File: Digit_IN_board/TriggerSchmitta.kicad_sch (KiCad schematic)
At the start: 6 parts, among them U5 HEF40106B, U6 HEF40106B, U7 HEF40106B

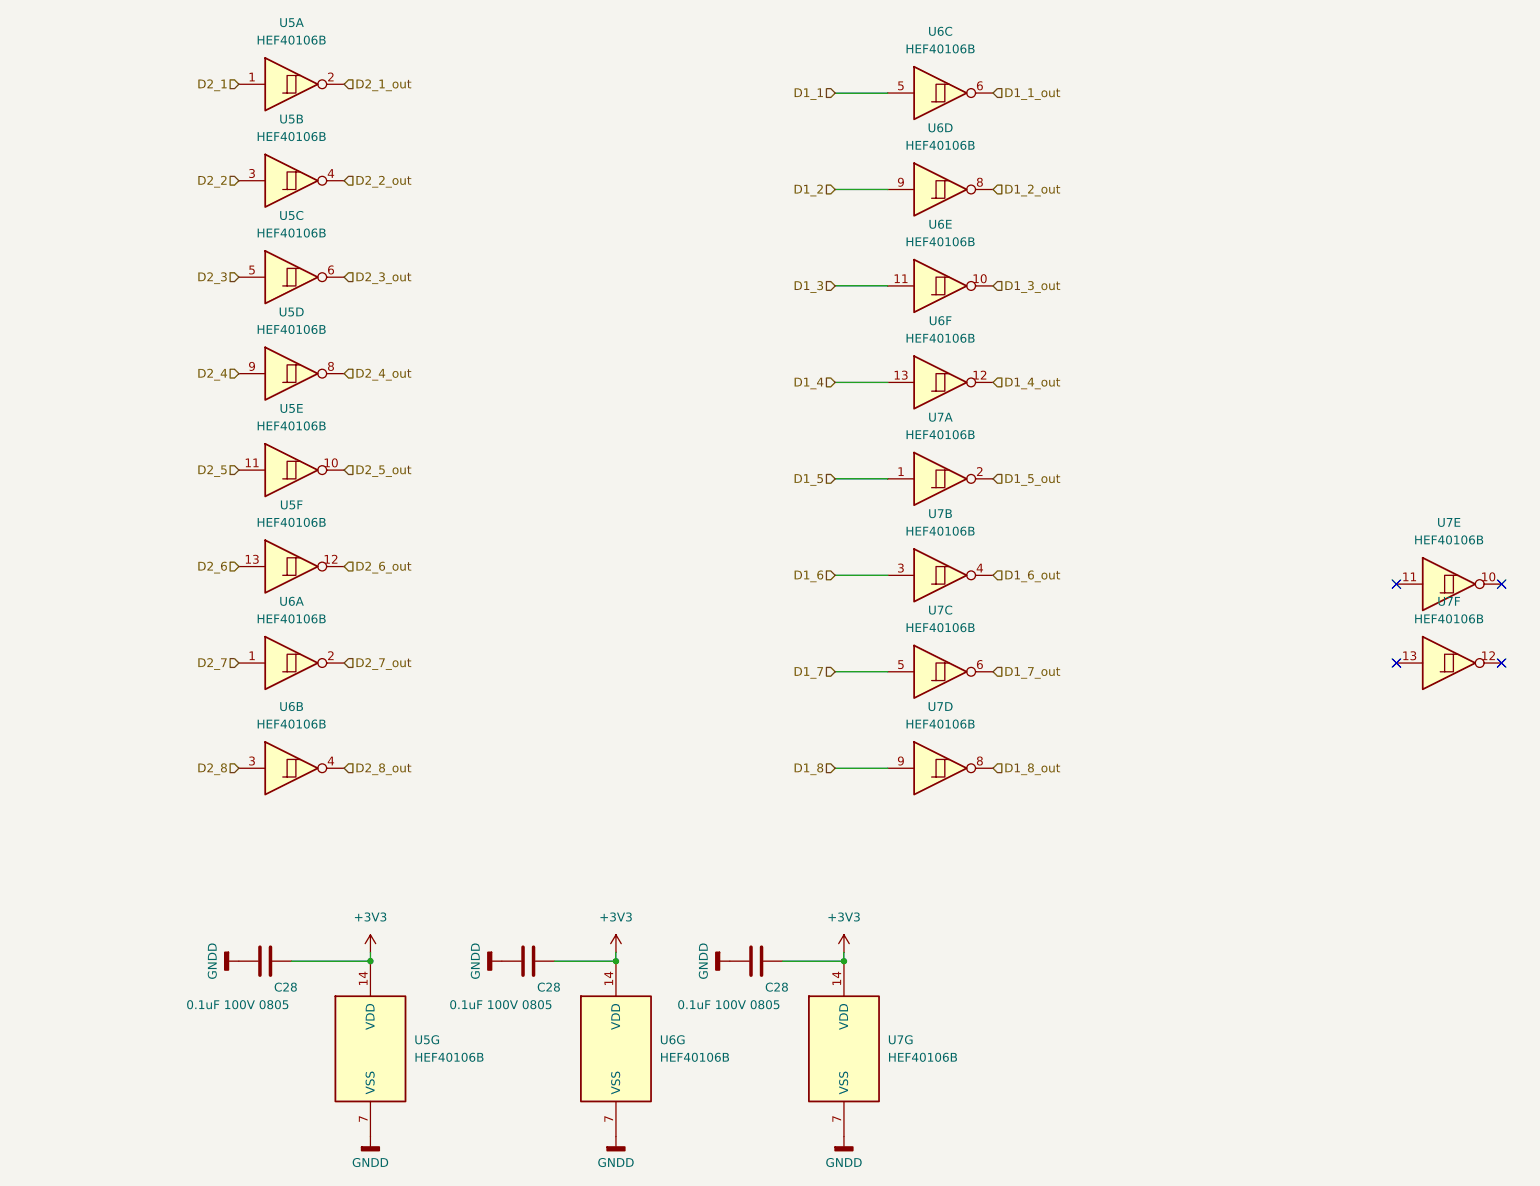
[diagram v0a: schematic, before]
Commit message: Modify Digit_IN, Motherbord, Step motors
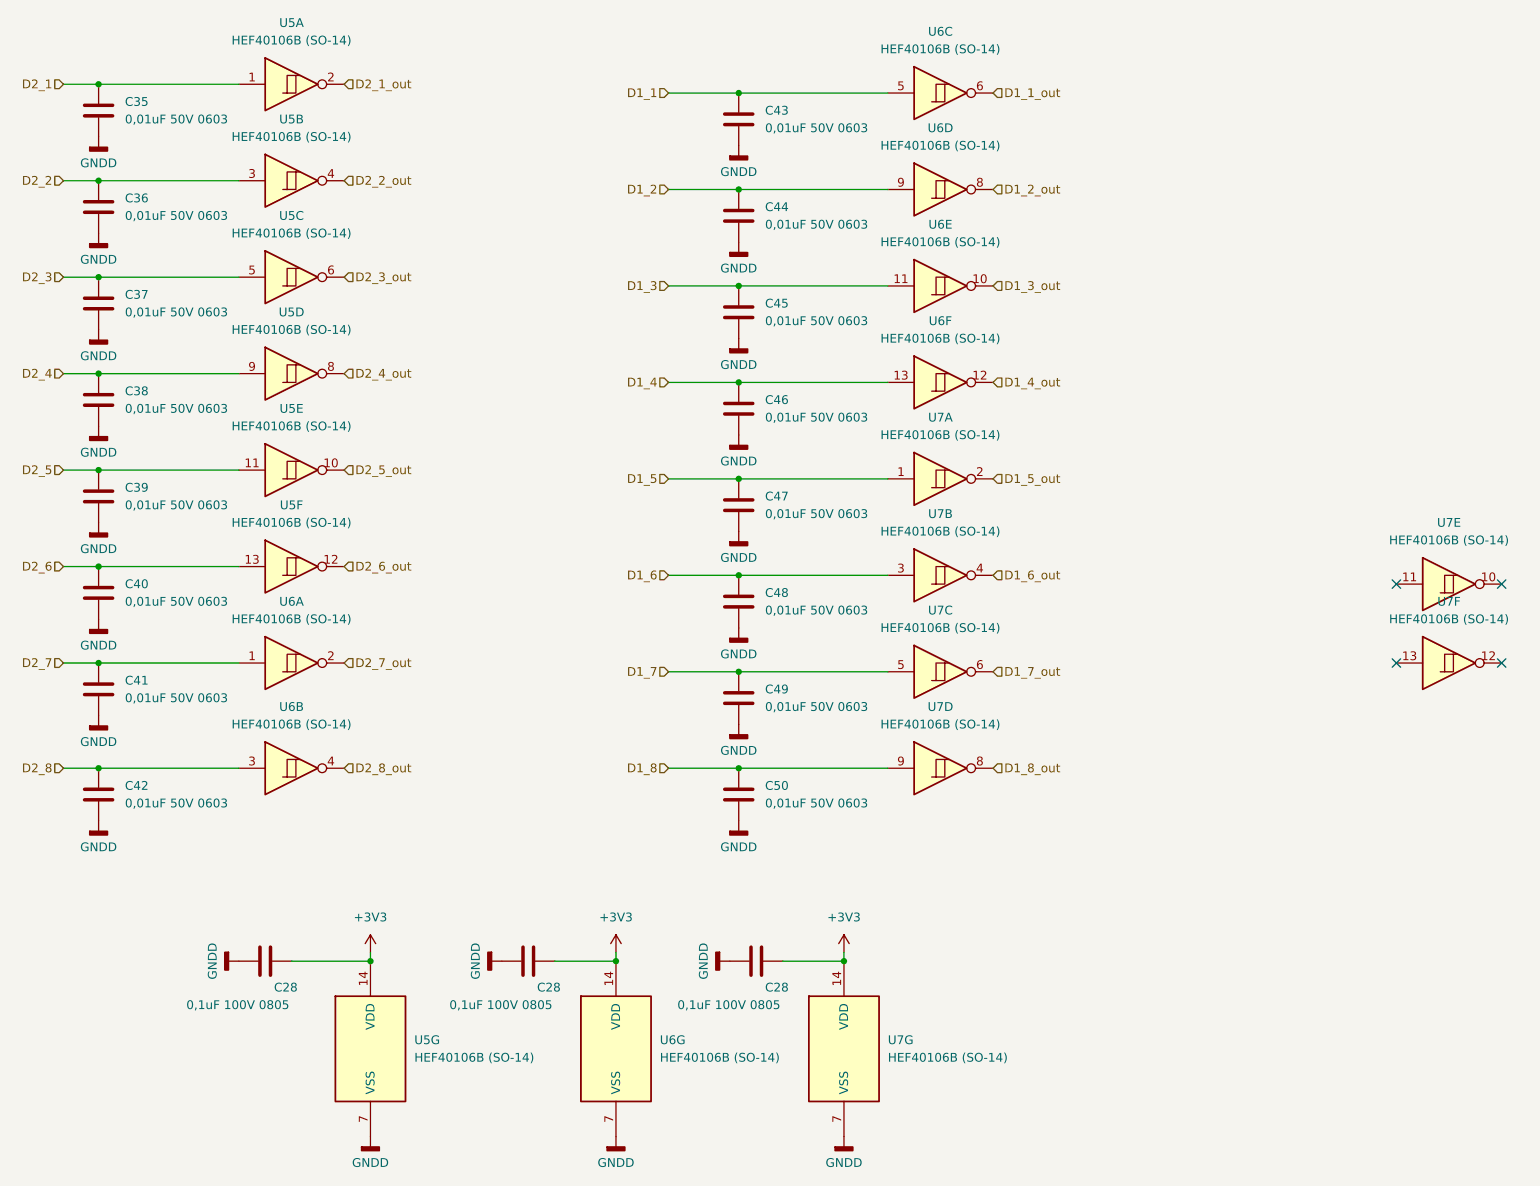
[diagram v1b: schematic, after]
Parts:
- added C35, C36, C37, C38, C39, C40, C41, C42, C43, C44, C45, C46, C47, C48, C49, C50: 0,01uF 50V 0603, PCM_Capacitor_SMD_US_Handsoldering_AKL:C_0603_1608Metric_Pad1.08x0.95mm, symbol Device:C
- C28: value 0.1uF 100V 0805 -> 0,1uF 100V 0805
- U5, U6, U7: value HEF40106B -> HEF40106B (SO-14)
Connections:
- net D1_1: now also C43.1
- net D1_2: now also C44.1
- net D1_3: now also C45.1
- net D1_4: now also C46.1
- net D1_5: now also C47.1
- net D1_6: now also C48.1
- net D1_7: now also C49.1
- net D1_8: now also C50.1
- net D2_1: now also C35.1
- net D2_2: now also C36.1
- net D2_3: now also C37.1
- net D2_4: now also C38.1
- net D2_5: now also C39.1
- net D2_6: now also C40.1
- net D2_7: now also C41.1
- net D2_8: now also C42.1
- net GNDD: now also C35.2, C36.2, C37.2, C38.2, C39.2, C40.2, C41.2, C42.2, C43.2, C44.2, C45.2, C46.2, C47.2, C48.2, C49.2, C50.2
